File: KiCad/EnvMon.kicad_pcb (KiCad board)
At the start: 2 copper layers, 44.5 x 37 mm, 17 parts, among them J1 USB-C, J2 DC, J3 GPIO, M1 D24V5F3-NoSHDN, M2 OLED1.5-RGB, M3 SCD30-4pin, U1 FT230XQ, U2 ESP32-WROOM-32

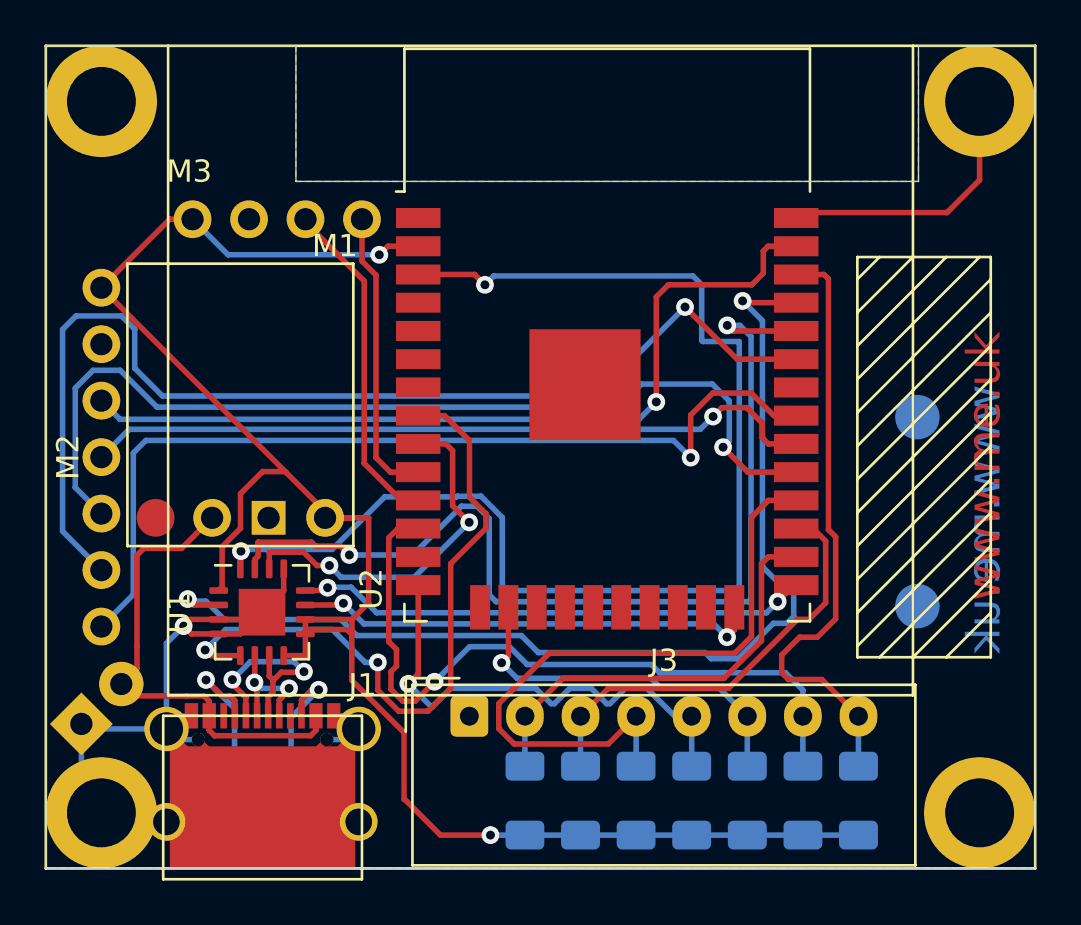
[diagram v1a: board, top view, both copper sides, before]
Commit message: Move DC connector
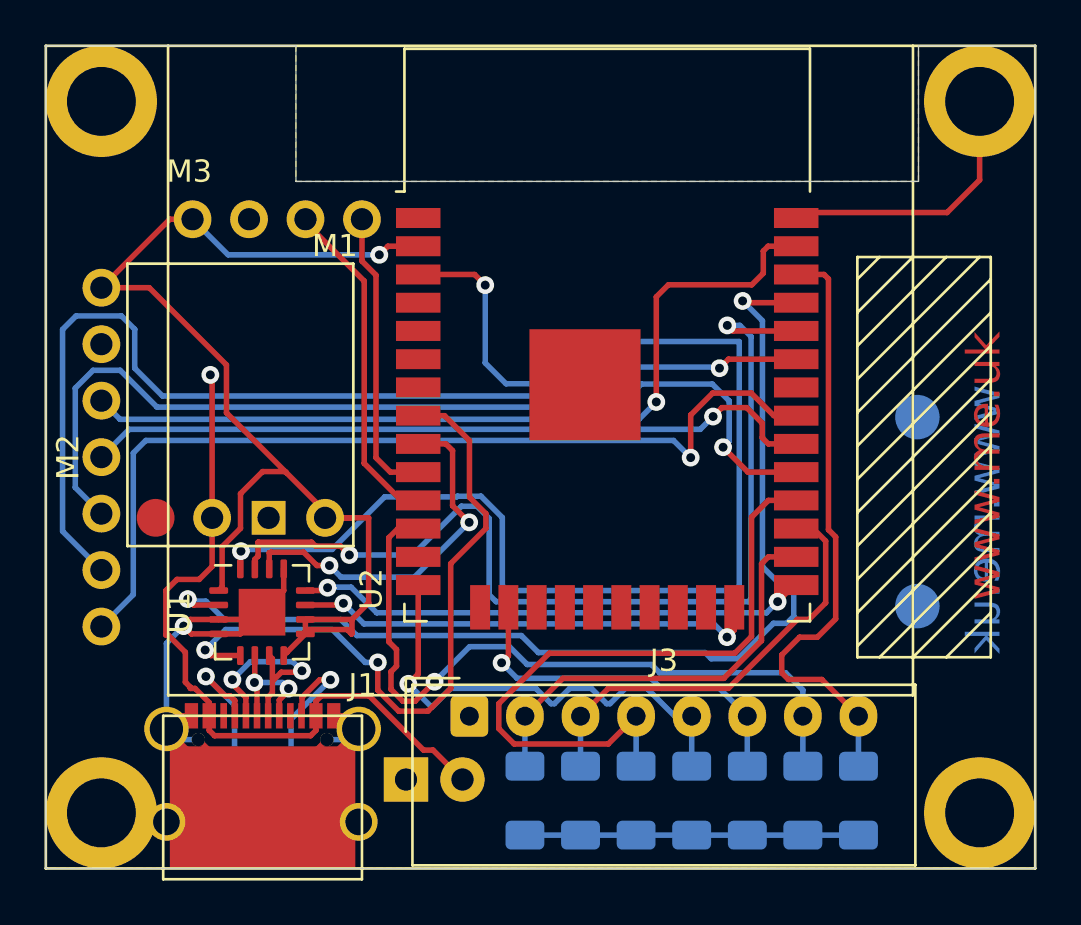
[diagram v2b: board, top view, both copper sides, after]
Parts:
- moved J2 14.8 mm to (106.2, 96.0), turned to 90 degrees
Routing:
- net +3V3: track 83.3 -> 69.5 mm, vias 2 -> 1
- net Net-(J1-PadA4): track 22.0 -> 33.6 mm, vias 0 -> 1
- net GND: track 74.8 -> 66.5 mm
- net OLED-DC: track 49.9 -> 48.0 mm
- net Net-(U1-Pad16): track 56.4 -> 58.2 mm
- net Net-(J1-PadB5): track 5.62 -> 7.06 mm

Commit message: Clearer QFN16 for soldering
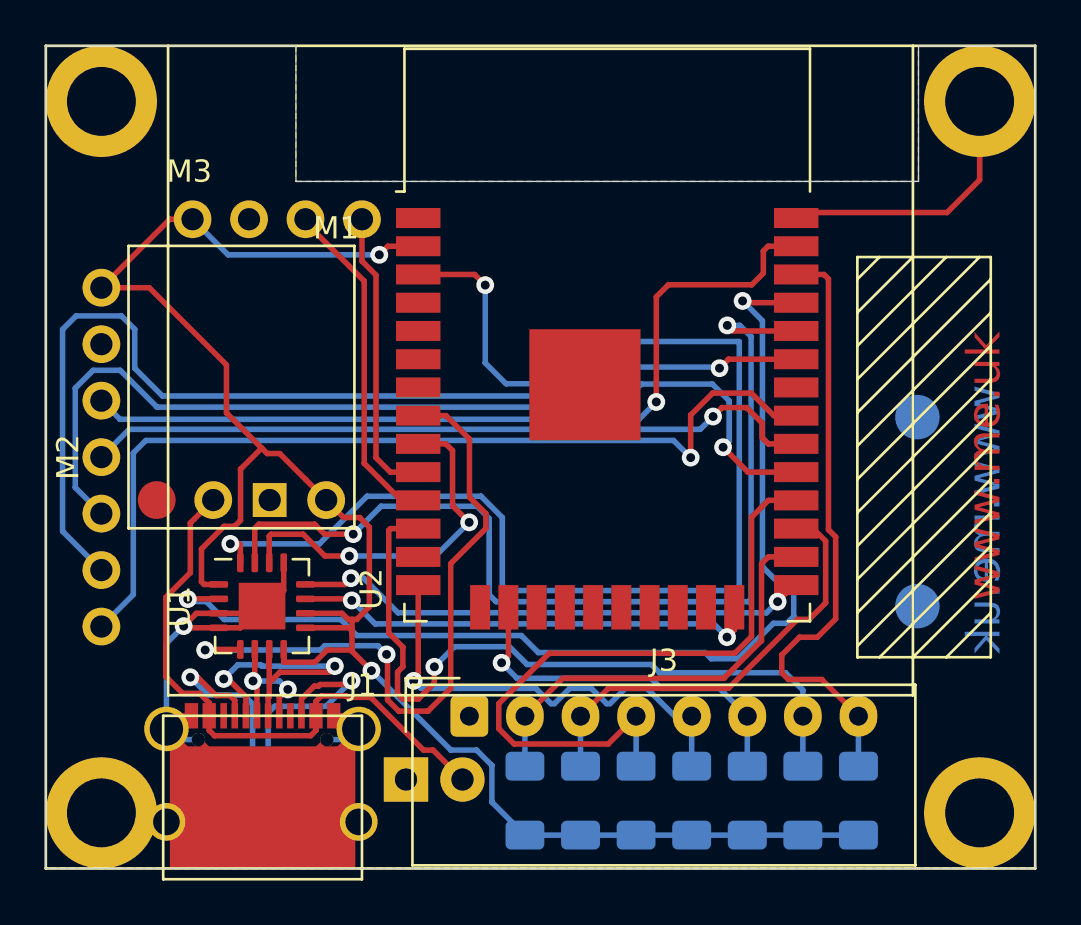
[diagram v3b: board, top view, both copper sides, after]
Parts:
- moved M1 0.80 mm to (98.8, 84.7)
- moved U1 0.27 mm to (99.7, 88.2)
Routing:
- net +3V3: track 69.5 -> 84.1 mm, vias 1 -> 2
- net Net-(J1-PadA4): track 33.6 -> 27.1 mm, vias 1 -> 0
- net Net-(J1-PadA7): track 9.85 -> 14.3 mm
- net Net-(J1-PadB5): track 7.06 -> 10.7 mm
- net Net-(J1-PadA5): track 7.01 -> 9.62 mm
- net IO4: track 22.8 -> 21.7 mm
- net Net-(U1-Pad16): track 58.2 -> 59.0 mm
- net Net-(J1-PadA6): track 5.81 -> 6.55 mm

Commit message: Revised easier to solder footprint
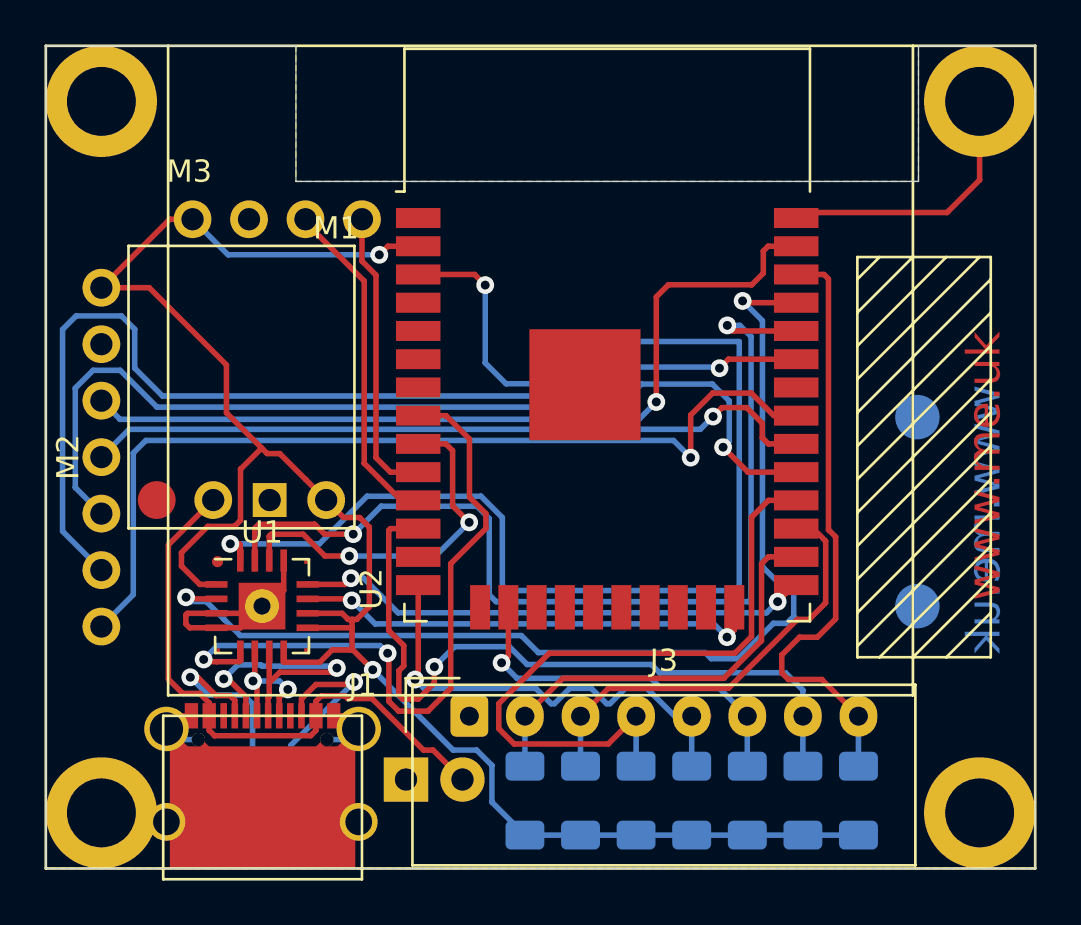
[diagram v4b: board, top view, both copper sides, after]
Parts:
- U1: footprint Package_DFN_QFN:QFN-16-1EP_4x4mm_P0.65mm_EP2.1x2.1mm -> RevK:QFN-16-(hand)-1EP_4x4mm_P0.65mm_EP2.1x2.1mm
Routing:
- net GND: track 66.5 -> 61.4 mm, vias 1 -> 0
- net Net-(J1-PadB5): track 10.7 -> 8.41 mm
- net +3V3: track 84.1 -> 85.2 mm
- net CBUS2: track 30.5 -> 31.3 mm

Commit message: Tweak tracks
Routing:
- net +3V3: track 85.2 -> 92.1 mm
- net Net-(J1-PadB5): track 8.41 -> 11.8 mm
- net Net-(U1-Pad15): track 45.0 -> 43.2 mm
- net CBUS1: track 23.0 -> 24.6 mm
- net CBUS0: track 23.3 -> 24.7 mm
- net IO4: track 21.6 -> 20.4 mm
- net Net-(U1-Pad16): track 59.0 -> 57.9 mm
- net OLED-MOSI: track 38.2 -> 37.4 mm
- net CBUS3: track 16.7 -> 16.0 mm
- net CBUS2: track 31.3 -> 30.7 mm
- net Net-(J1-PadA4): track 27.0 -> 27.5 mm

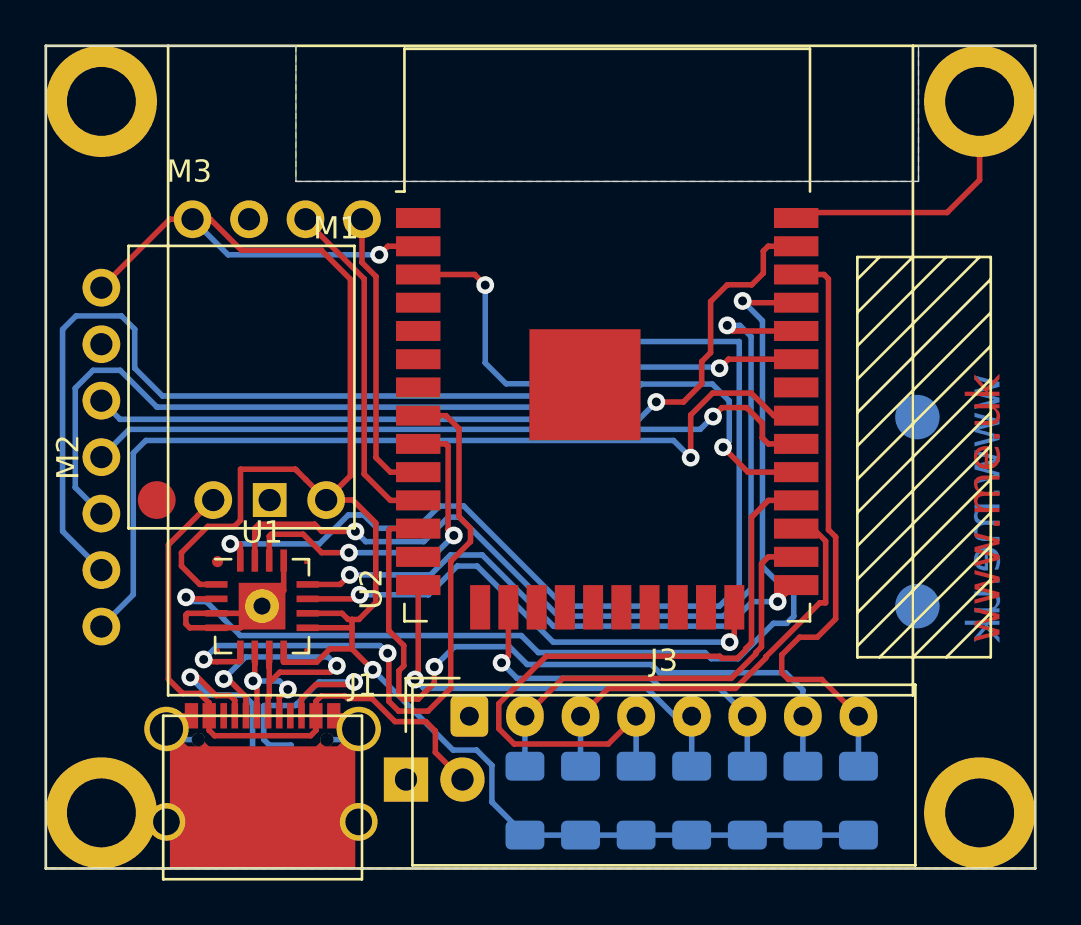
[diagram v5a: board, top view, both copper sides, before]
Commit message: Way more clearance around regulator pads
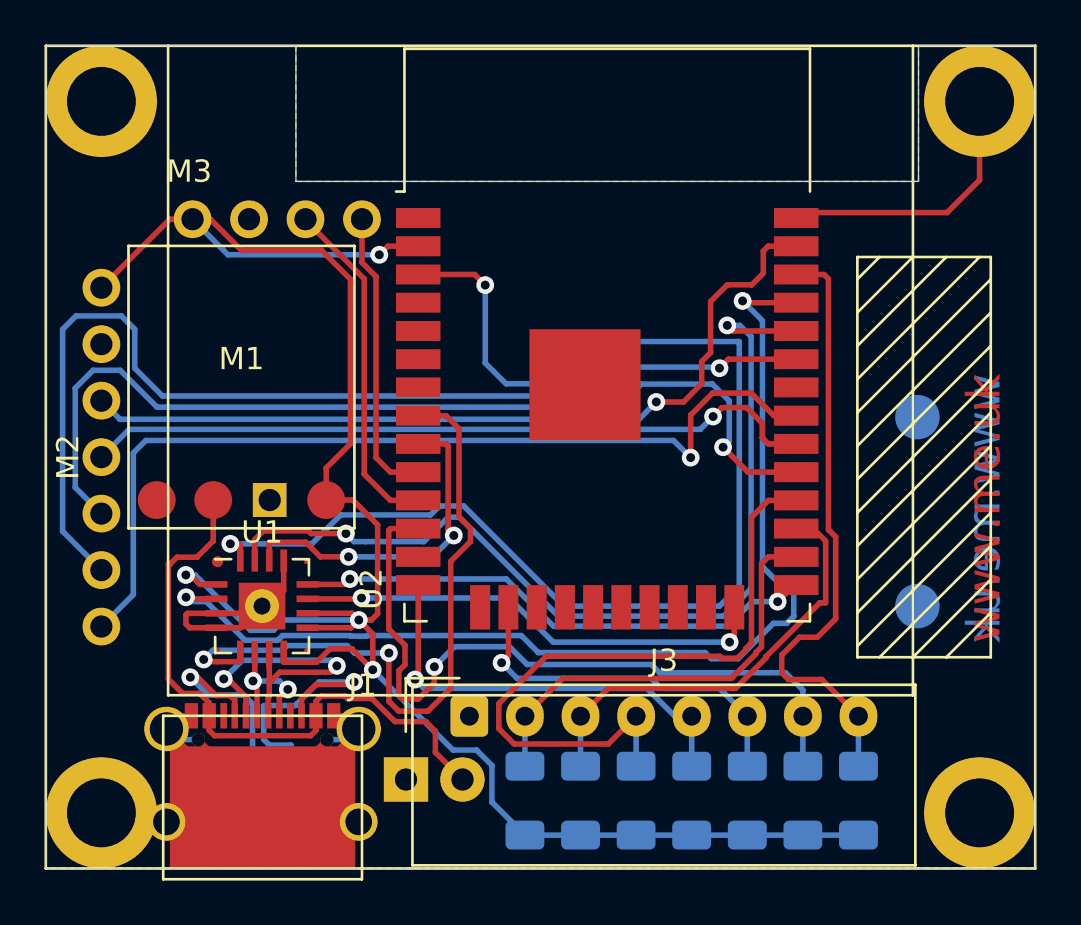
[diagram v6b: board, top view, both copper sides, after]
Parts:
- M1: footprint RevK:D24V5F3-NoSHDN -> RevK:D24V5F3-SMD-Like
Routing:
- net CBUS1: track 24.6 -> 23.4 mm
- net Net-(U1-Pad15): track 43.2 -> 42.3 mm
- net CBUS0: track 24.7 -> 23.8 mm
- net CBUS3: track 16.0 -> 15.3 mm
- net Net-(J1-PadA4): track 27.5 -> 28.1 mm
- net +3V3: vias 2 -> 4

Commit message: Clearance around FTDI
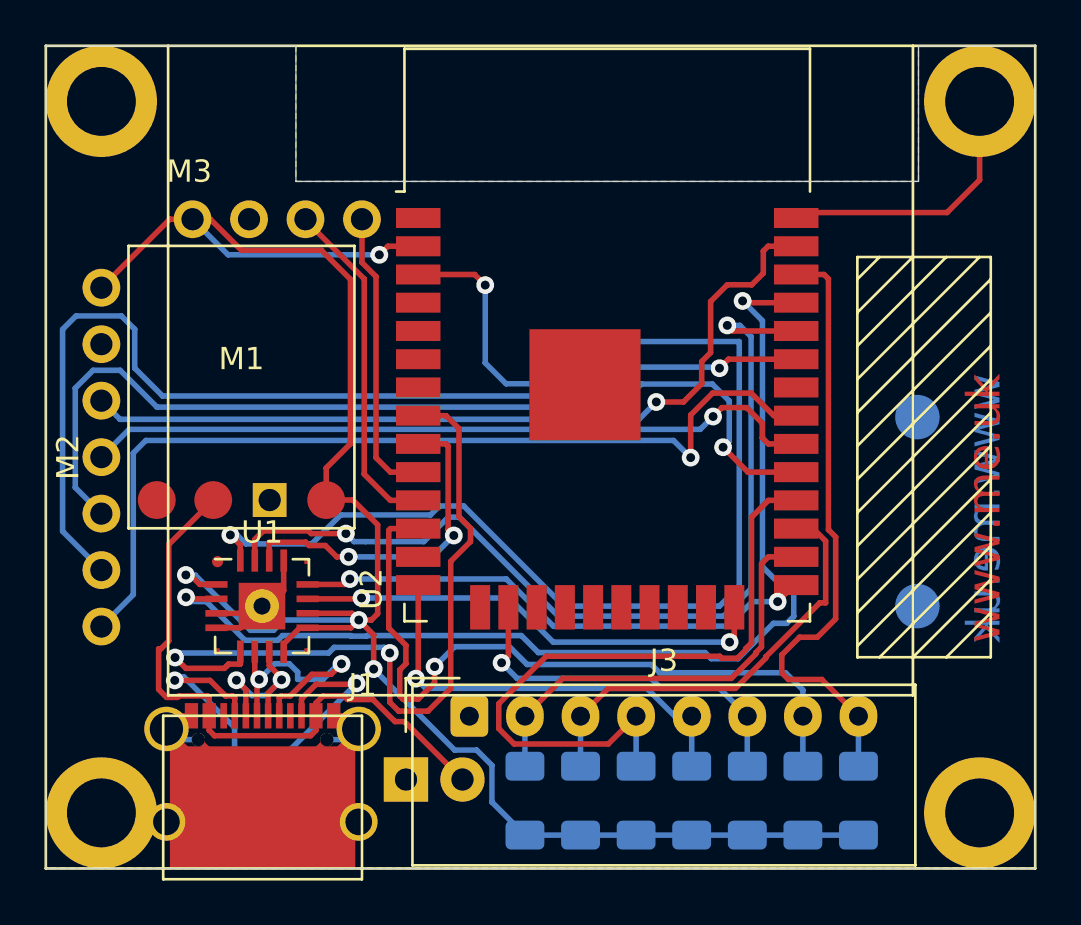
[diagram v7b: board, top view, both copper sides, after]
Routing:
- net Net-(J1-PadA7): track 14.6 -> 7.75 mm
- net Net-(J1-PadA6): track 6.55 -> 12.0 mm
- net +3V3: track 92.1 -> 88.3 mm
- net Net-(J1-PadB5): track 11.8 -> 8.48 mm
- net GND: track 61.4 -> 58.2 mm
- net CBUS2: track 30.7 -> 33.8 mm

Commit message: Logo
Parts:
- added 1: AJK, RevK:AJK, B.Cu at (134.0, 73.4)
- added ~1: AJK, RevK:AJK, F.Cu at (134.0, 72.4)
